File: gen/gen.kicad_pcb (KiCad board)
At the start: 2 copper layers, 40.6 x 40.6 mm, 16 parts

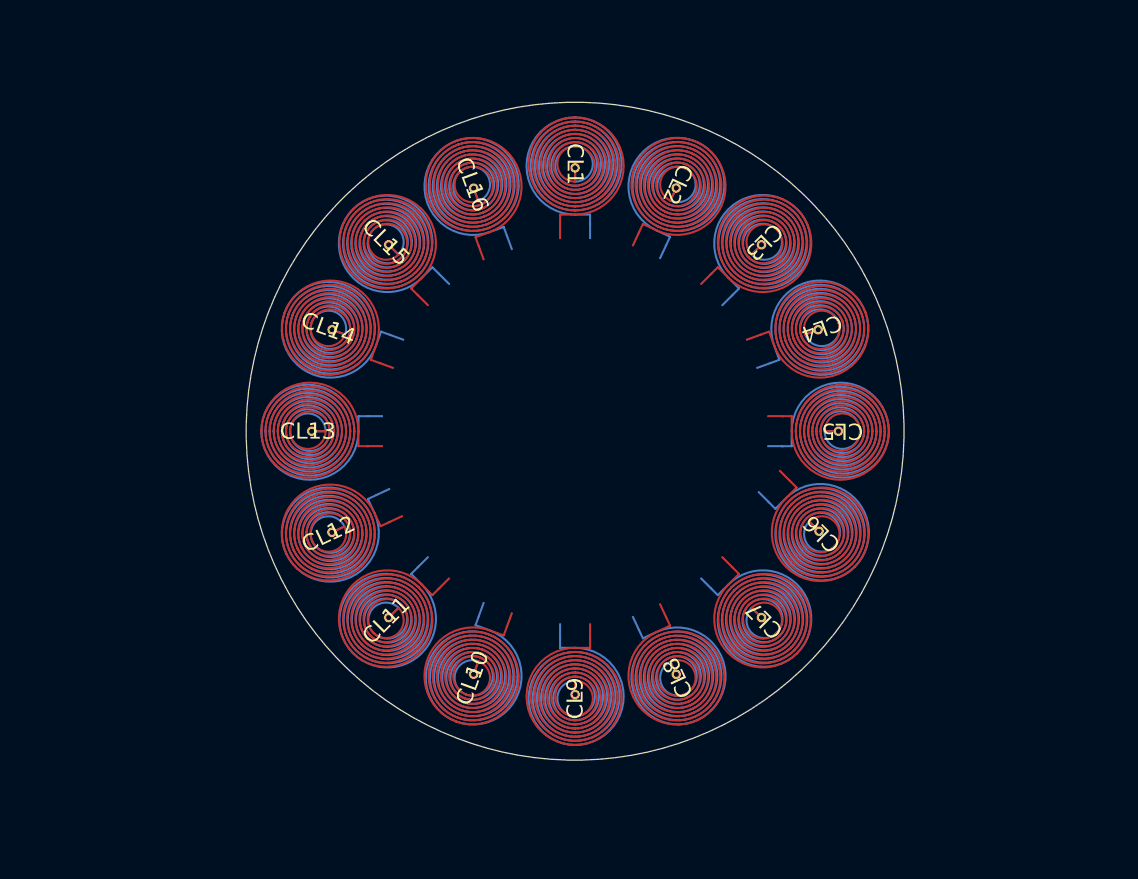
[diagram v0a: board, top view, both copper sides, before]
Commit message: Connected All Coils
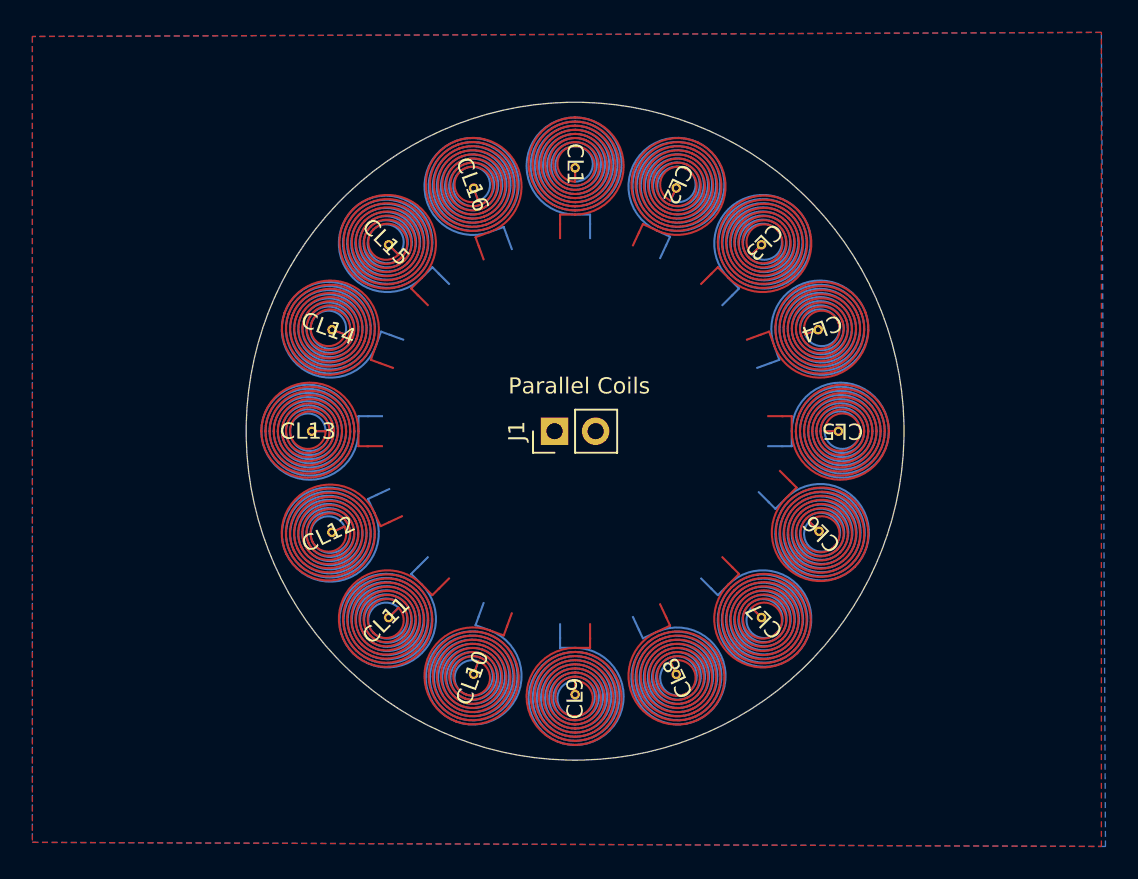
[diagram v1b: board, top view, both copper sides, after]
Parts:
- added J1: Conn_01x02_Socket, Connector_PinHeader_2.54mm:PinHeader_1x02_P2.54mm_Vertical, F.Cu at (151.1, 101.6)
- CL1, CL10, CL11, CL12, CL13, CL14, CL15, CL16, CL2, CL3, CL4, CL5, CL6, CL7, CL8, CL9: value SMALL_COIL -> L
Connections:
- CL1 pad 1: (no net) -> Net-(J1-Pin_1)
- CL1 pad 2: (no net) -> Net-(J1-Pin_2)
- CL10 pad 1: (no net) -> Net-(J1-Pin_1)
- CL10 pad 2: (no net) -> Net-(J1-Pin_2)
- CL11 pad 1: (no net) -> Net-(J1-Pin_1)
- CL11 pad 2: (no net) -> Net-(J1-Pin_2)
- CL12 pad 1: (no net) -> Net-(J1-Pin_1)
- CL12 pad 2: (no net) -> Net-(J1-Pin_2)
- CL13 pad 1: (no net) -> Net-(J1-Pin_1)
- CL13 pad 2: (no net) -> Net-(J1-Pin_2)
- CL14 pad 1: (no net) -> Net-(J1-Pin_1)
- CL14 pad 2: (no net) -> Net-(J1-Pin_2)
- CL15 pad 1: (no net) -> Net-(J1-Pin_1)
- CL15 pad 2: (no net) -> Net-(J1-Pin_2)
- CL16 pad 1: (no net) -> Net-(J1-Pin_1)
- CL16 pad 2: (no net) -> Net-(J1-Pin_2)
- CL2 pad 1: (no net) -> Net-(J1-Pin_1)
- CL2 pad 2: (no net) -> Net-(J1-Pin_2)
- CL3 pad 1: (no net) -> Net-(J1-Pin_1)
- CL3 pad 2: (no net) -> Net-(J1-Pin_2)
- CL4 pad 1: (no net) -> Net-(J1-Pin_1)
- CL4 pad 2: (no net) -> Net-(J1-Pin_2)
- CL5 pad 1: (no net) -> Net-(J1-Pin_1)
- CL5 pad 2: (no net) -> Net-(J1-Pin_2)
- CL6 pad 1: (no net) -> Net-(J1-Pin_1)
- CL6 pad 2: (no net) -> Net-(J1-Pin_2)
- CL7 pad 1: (no net) -> Net-(J1-Pin_1)
- CL7 pad 2: (no net) -> Net-(J1-Pin_2)
- CL8 pad 1: (no net) -> Net-(J1-Pin_1)
- CL8 pad 2: (no net) -> Net-(J1-Pin_2)
- CL9 pad 1: (no net) -> Net-(J1-Pin_1)
- CL9 pad 2: (no net) -> Net-(J1-Pin_2)
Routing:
- added copper zone on F.Cu, net Net-(J1-Pin_1)
- added copper zone on B.Cu, net Net-(J1-Pin_2)
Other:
- board text added: "Parallel Coils"
